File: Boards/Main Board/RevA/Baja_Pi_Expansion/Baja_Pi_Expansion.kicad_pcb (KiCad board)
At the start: 2 copper layers, 25 parts, among them J1 Conn_02x10_Counter_Clockwise, J2 Conn_02x12_Counter_Clockwise, J3 Screw_Terminal_01x04, J4 Conn_02x20_Odd_Even, J5 Conn_01x03_Male, J6 Screw_Terminal_01x07, U1 HDSP-7403

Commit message: Roughed out Main Board PCB
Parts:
- D1: footprint LED_SMD:LED_1812_4532Metric -> Custom Footprints:LED_0805_2012Metric
- J4: moved to B.Cu
- moved J2 218.7 mm to (240.5, 84.0)
- moved D1 201.0 mm to (230.5, 123.5)
- moved C3 196.3 mm to (226.5, 94.5)
- moved VR1 195.1 mm to (219.7, 98.0)
- moved C4 195.0 mm to (227.4, 98.0)
- moved C2 192.5 mm to (226.5, 101.5)
- moved C1 191.4 mm to (213.5, 98.0), turned to 90 degrees
- moved U1 184.0 mm to (225.1, 77.5), turned to 90 degrees
- moved J3 180.7 mm to (211.0, 122.0), turned to 90 degrees
- moved J6 172.3 mm to (187.0, 122.0), turned to 90 degrees
- moved R6 164.4 mm to (185.0, 100.5), turned to 270 degrees
- moved R7 163.9 mm to (190.0, 98.0), turned to 90 degrees
- moved J4 153.2 mm to (168.4, 72.6), turned to 270 degrees
- moved J5 149.6 mm to (187.0, 109.0), turned to 90 degrees
- moved H4 145.8 mm to (241.5, 122.5)
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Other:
- board outline added: 85 x 56 mm
- board text added: "# of Boards"
- board text added: "+5V"
- board text added: "ANALOG"
- board text added: "BRAKES"
- board text added: "DIGITAL"
- board text added: "GND"
- board text added: "JLCJLCJLCJLC"
- board text added: "Left to do: RE-ORIENT HEADER (TELL CHRIS) Place PI Header and Orient Route"
- board text added: "PWR"
- board text added: "Pull Down"
- board text added: "Pull Up"
- board text added: "RIT Baja SDAQ Main Board Revision A Adam Seidman (732) 882-9717"
- board text added: "VCC"

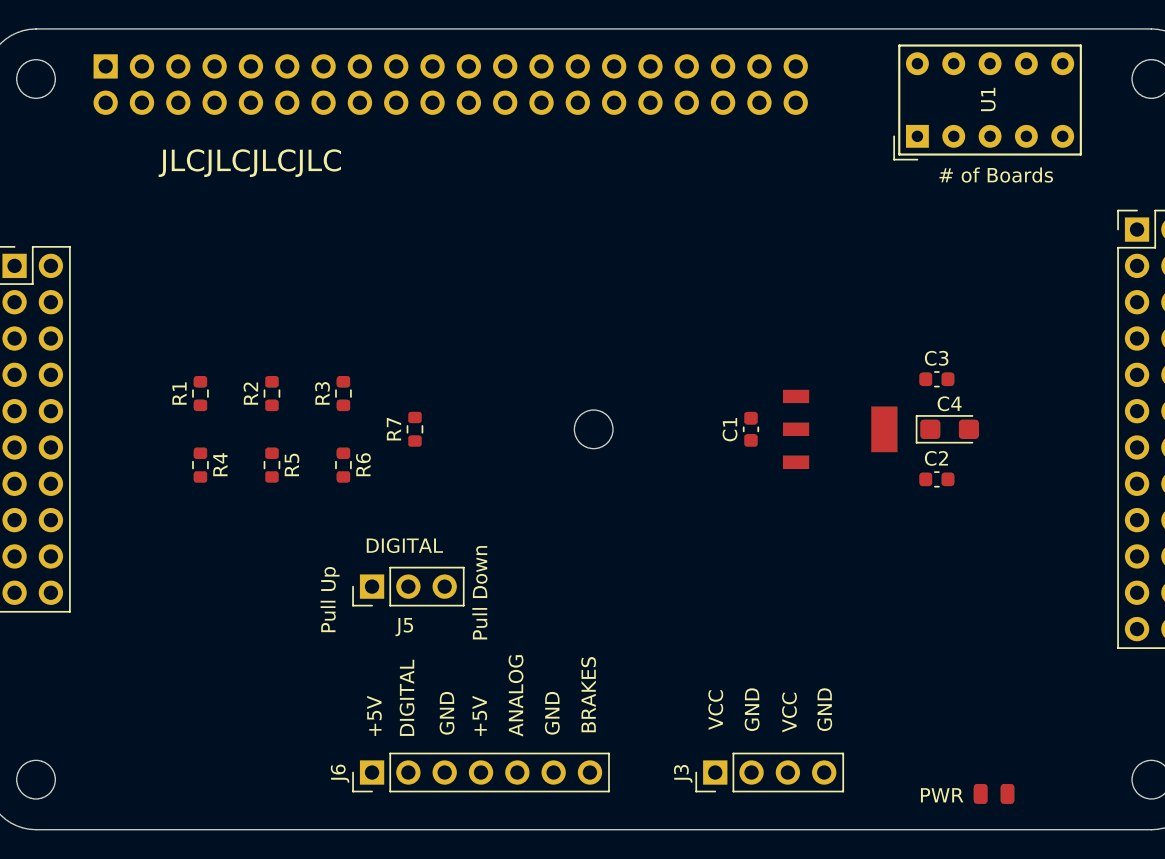
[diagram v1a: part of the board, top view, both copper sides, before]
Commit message: Placed Pi Header and Created .dsn File for Main Board
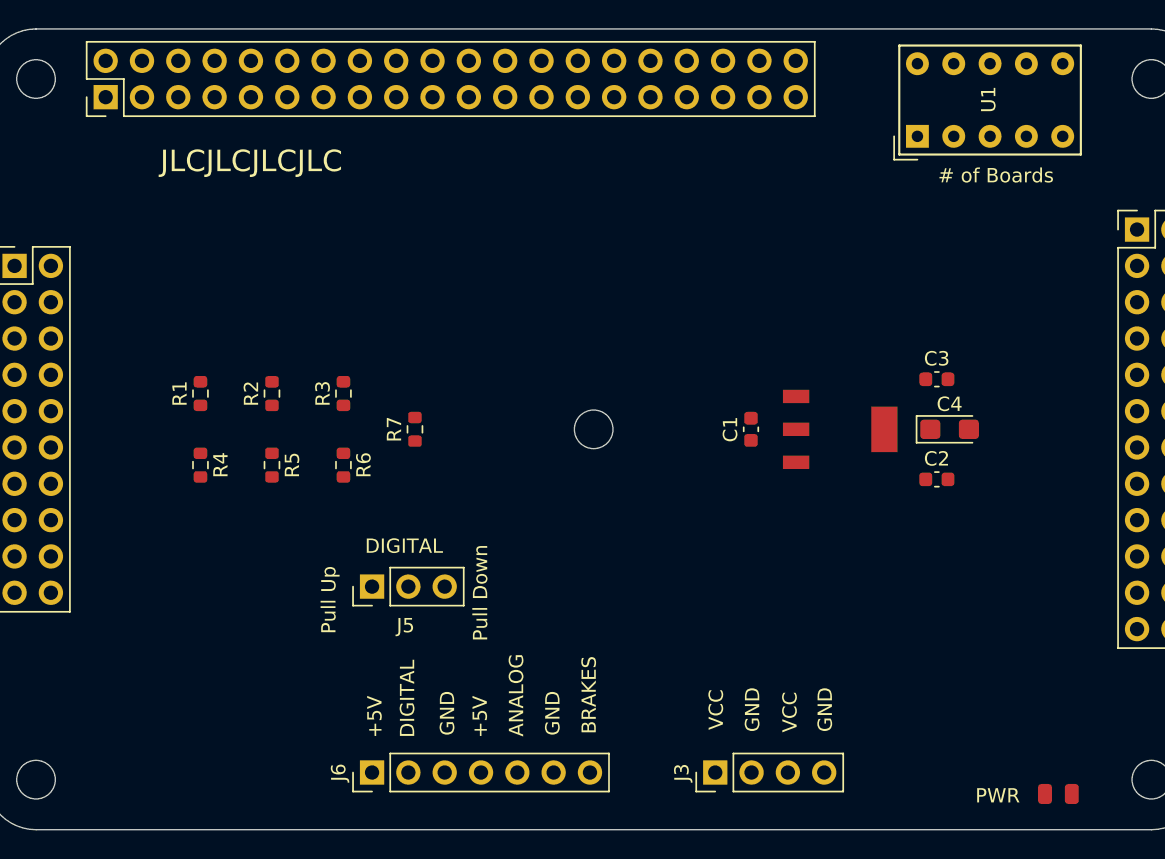
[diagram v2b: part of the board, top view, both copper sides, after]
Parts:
- J4: moved to F.Cu
- moved D1 4.50 mm to (235.0, 123.5)
- moved J4 2.15 mm to (168.4, 74.8), turned to 90 degrees
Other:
- board text added: "Left to do: Route"
- board text removed: "Left to do: RE-ORIENT HEADER (TELL CHRIS) Place PI Header and Orient Route"

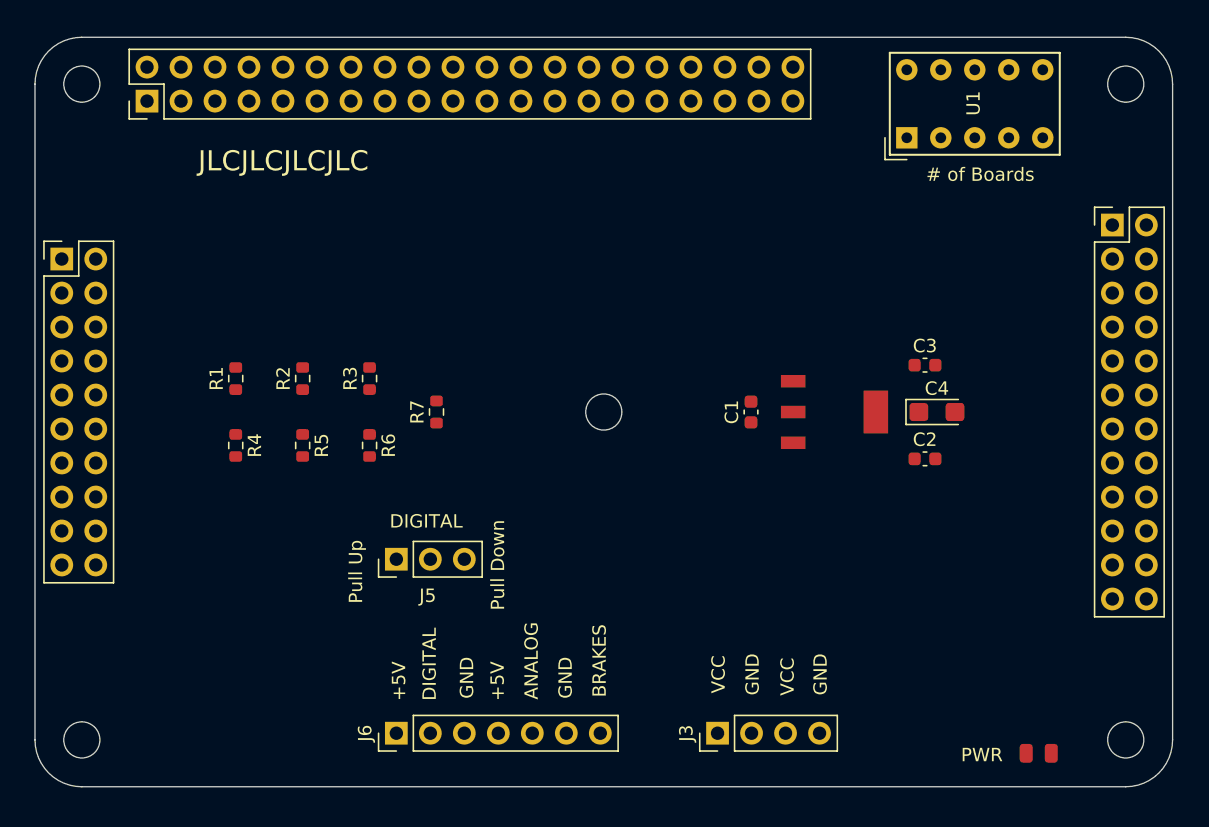
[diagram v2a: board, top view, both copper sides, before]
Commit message: Updated .dsn Files and Power Planes/Keepouts for Main Board
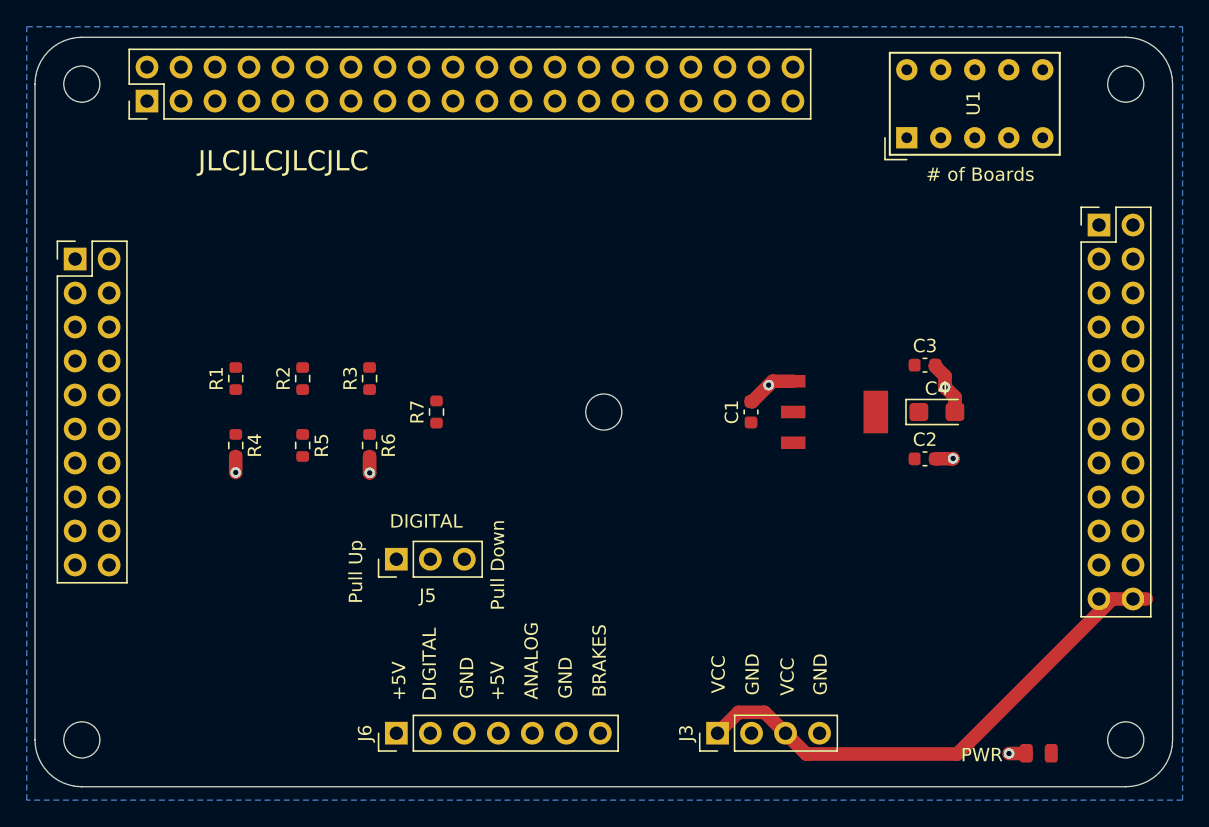
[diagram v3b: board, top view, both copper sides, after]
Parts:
- moved J1 1.00 mm to (163.0, 86.6)
- moved J2 1.00 mm to (239.5, 84.0)
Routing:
- net /vcc: track 0.00 -> 38.8 mm
- net /gnd: track 0.00 -> 12.9 mm, vias 0 -> 6
- added copper zone on B.Cu, net /gnd

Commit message: Finished Main Board Routing
Made 4 Layers
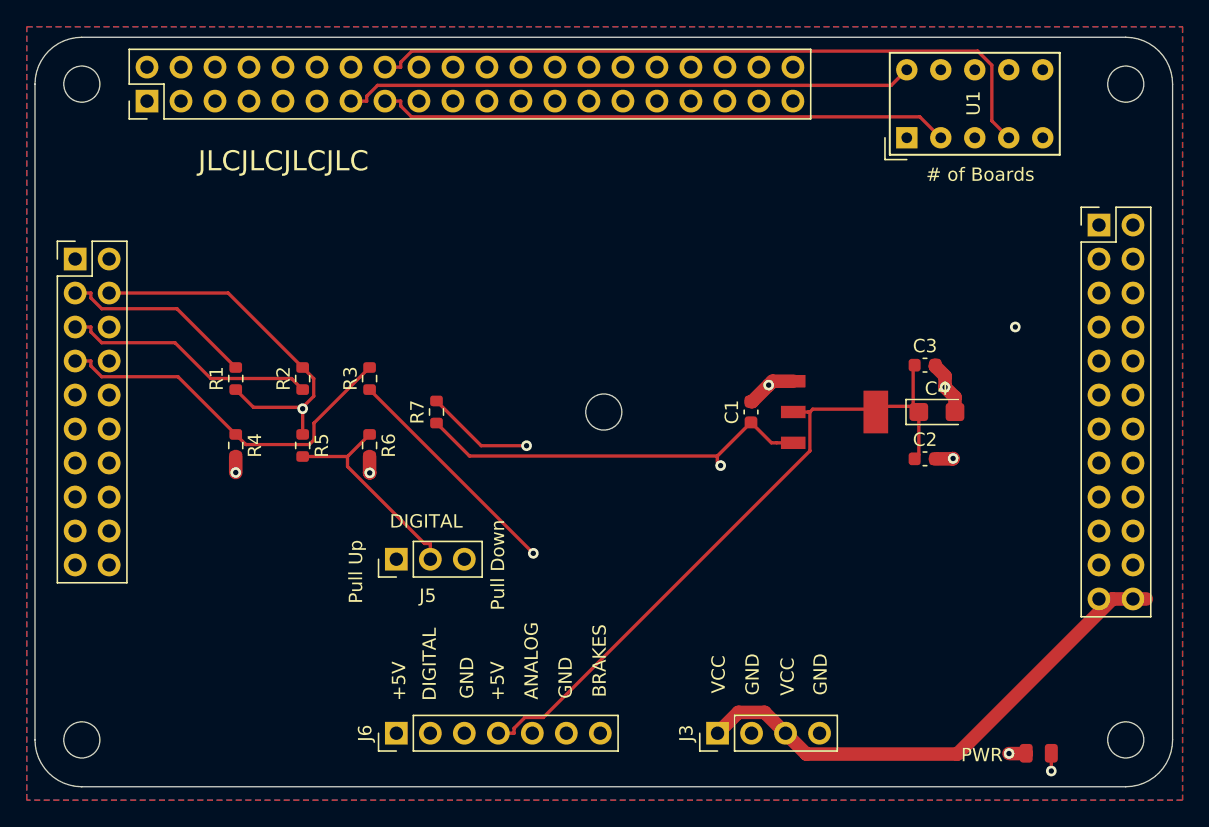
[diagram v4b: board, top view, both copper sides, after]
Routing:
- net /5v: track 0.00 -> 137.1 mm, vias 0 -> 1
- net /dig_in: track 0.00 -> 129.4 mm
- net /analog_in: track 0.00 -> 103.6 mm
- net /gpio8: track 0.00 -> 95.0 mm
- net /gpio7: track 0.00 -> 93.5 mm
- net /gpio6: track 0.00 -> 83.3 mm
- net /gpio11: track 0.00 -> 79.5 mm
- net /miso: track 0.00 -> 72.3 mm
- net /reset: track 0.00 -> 64.4 mm
- net /gpio10: track 0.00 -> 58.8 mm
- net Net-(D1-Pad2): track 0.00 -> 58.7 mm, vias 0 -> 2
- net /gpio4: track 0.00 -> 58.3 mm
- net /3v3: track 0.00 -> 57.5 mm
- net /gpio9: track 0.00 -> 55.6 mm
- net /spi_ce0: track 0.00 -> 53.7 mm
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- added copper zone on F.Cu, net /vcc
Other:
- copper layers 2 -> 4
